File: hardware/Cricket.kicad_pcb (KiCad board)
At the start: 2 copper layers, 67.5 x 38.5 mm, 14 parts, among them J1 S2B-XH-A, Q1 RQ6C065BCTCR, SW1 SW_SPDT, U1 Seeed Xiao ESP32C3, U2 DFR0299

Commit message: v0.2 tapeout
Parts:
- D1: footprint LED_SMD:LED_PLCC_2835_Handsoldering -> Cricket_footprints:LED_PLCC_2835
- R1, R2, R3, R4, R5, R6, R7: footprint Resistor_SMD:R_1206_3216Metric_Pad1.30x1.75mm_HandSolder -> Cricket_footprints:R_1206_3216Metric_Pad1.30x1.75mm_HandSolder
- U1: footprint RF_Module:MCU_Seeed_ESP32C3 -> Cricket_footprints:Seeed_Xiao_ESP32C3
- moved LS1 3.60 mm to (146.5, 79.2)
- moved U1 3.60 mm to (126.1, 72.9)
- moved R6 3.60 mm to (112.0, 70.4)
- moved R7 3.60 mm to (112.0, 67.7)
- moved SW1 3.60 mm to (108.5, 63.0)
- moved D1 3.60 mm to (142.3, 90.0)
- moved Q1 3.60 mm to (145.7, 64.9)
- moved R1 3.60 mm to (140.4, 65.9)
- moved R2 3.60 mm to (140.4, 72.9)
- moved R3 3.60 mm to (140.4, 75.5)
- moved R4 3.60 mm to (140.4, 78.0)
- moved R5 3.60 mm to (140.4, 80.5)
- moved U2 3.60 mm to (159.2, 72.9)
- moved J1 3.00 mm to (106.0, 85.5)
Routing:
- net VCC: track 20.5 -> 22.5 mm
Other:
- board size 67.5 x 38.5 mm -> 73.5 x 40.5 mm
- board text added: "Blake Jones, September 2024"
- board text added: "Fire Cricket v0.2"
- board text removed: "Blake Jones, August 2024"
- board text removed: "Fire Cricket v0.1"

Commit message: Hardware for v0.2a (PCBA)
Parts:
- D1: footprint Cricket_footprints:LED_PLCC_2835 -> LED_SMD:LED_PLCC_2835
- U1: footprint Cricket_footprints:Seeed_Xiao_ESP32C3 -> RF_Module:MCU_Seeed_ESP32C3; moved to B.Cu
- turned U1 to 180 degrees
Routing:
- net GND: track 44.6 -> 50.2 mm, vias 17 -> 20
- net Net-(SW1-C): track 28.4 -> 26.2 mm, vias 1 -> 0
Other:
- board text added: "Fire Cricket v0.2a"
- board text removed: "Fire Cricket v0.2"

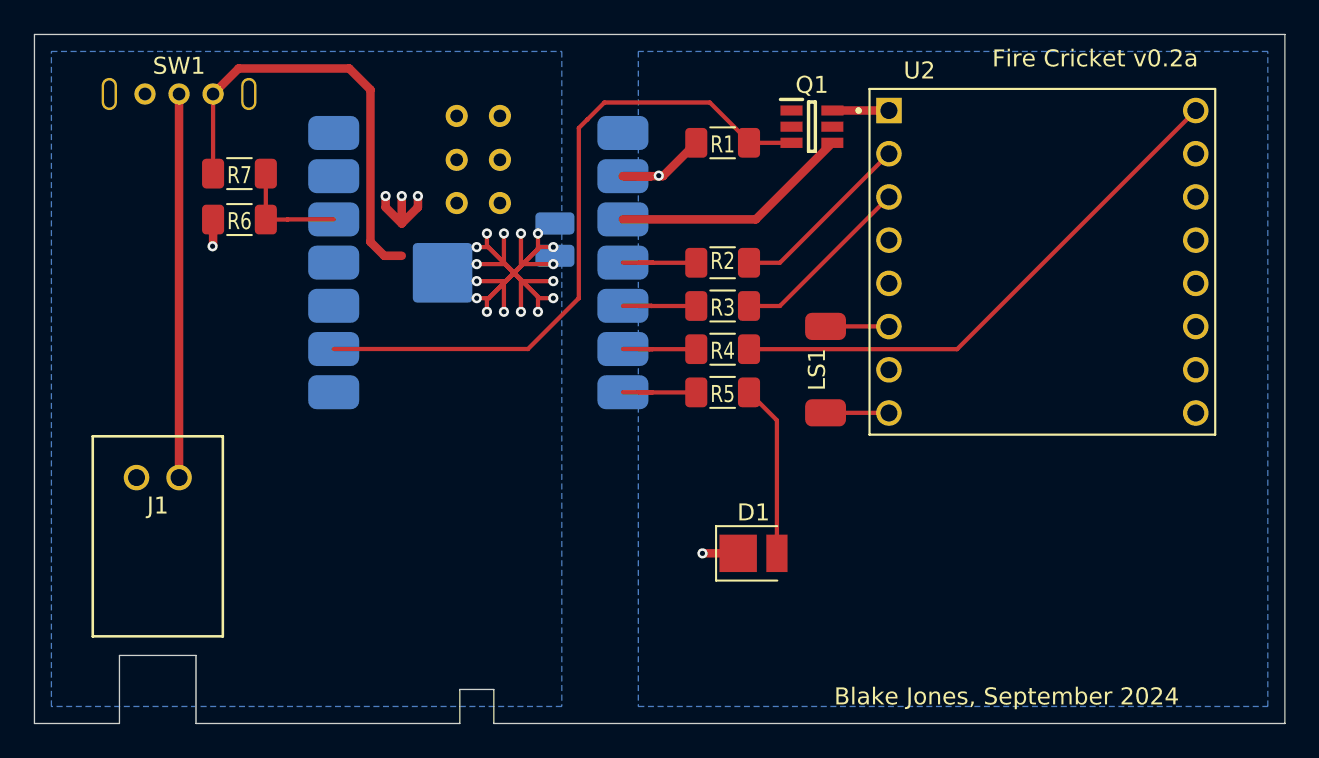
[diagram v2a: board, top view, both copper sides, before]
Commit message: Revert hardware to v0.2, since I'm using that
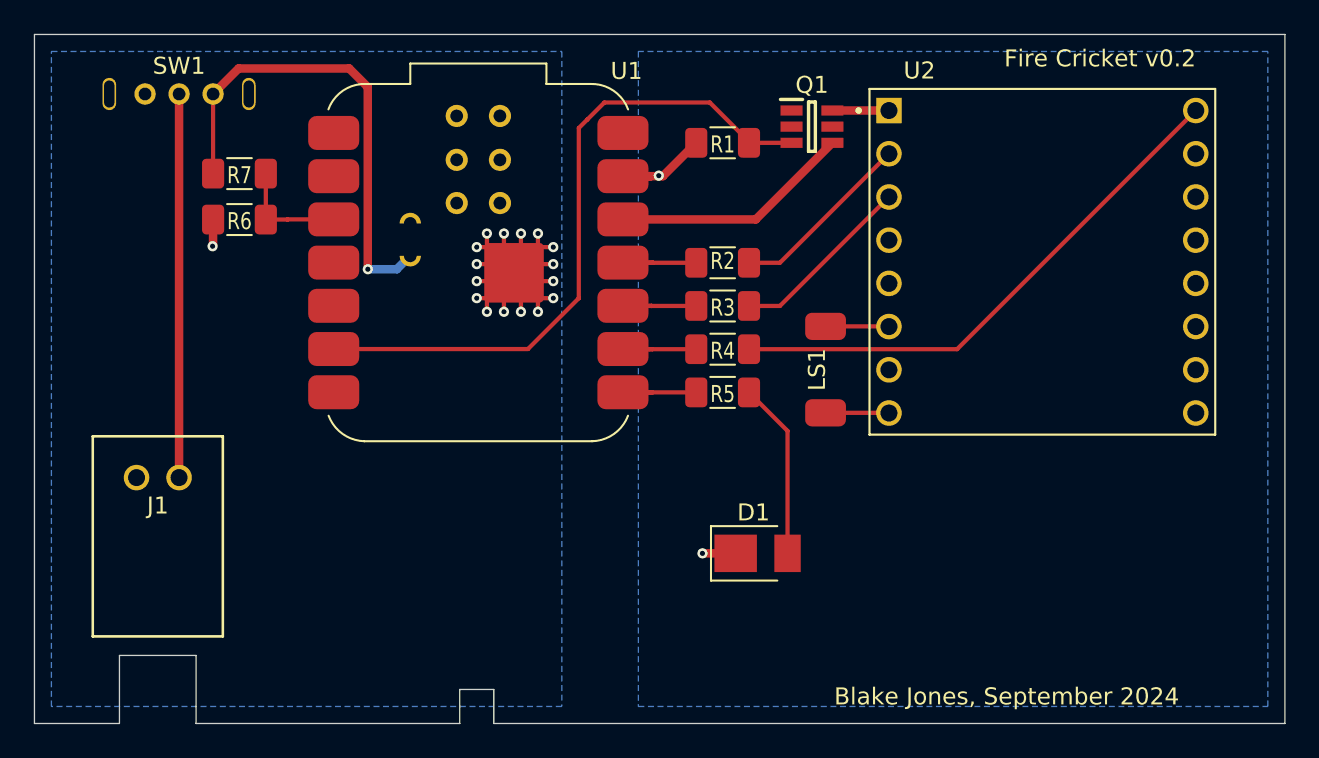
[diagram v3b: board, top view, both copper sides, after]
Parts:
- D1: footprint LED_SMD:LED_PLCC_2835 -> Cricket_footprints:LED_PLCC_2835
- U1: footprint RF_Module:MCU_Seeed_ESP32C3 -> Cricket_footprints:Seeed_Xiao_ESP32C3; moved to F.Cu
- turned U1 to 0 degrees
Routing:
- net GND: track 50.2 -> 44.6 mm, vias 20 -> 17
- net Net-(SW1-C): track 26.2 -> 28.4 mm, vias 0 -> 1
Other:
- board text added: "Fire Cricket v0.2"
- board text removed: "Fire Cricket v0.2a"
